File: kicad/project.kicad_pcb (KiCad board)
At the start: 2 copper layers, 59 x 59 mm, 36 parts, among them J1 Conn_01x05, J2 Conn_01x01, SW1 SW_SPDT, SW2 SW_SPDT, SW3 SW_Push, U1 STM32L031F4Px

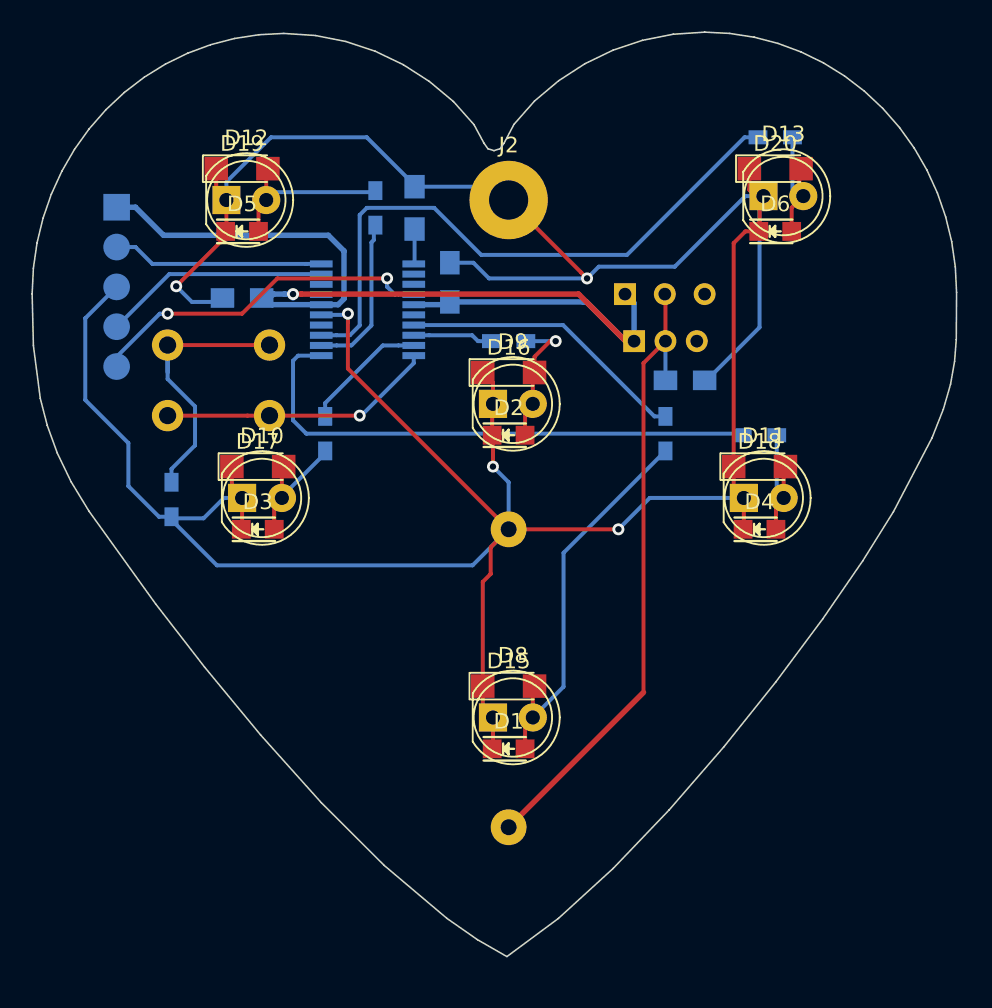
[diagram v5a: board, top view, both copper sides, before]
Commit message: Reverse polarity protection
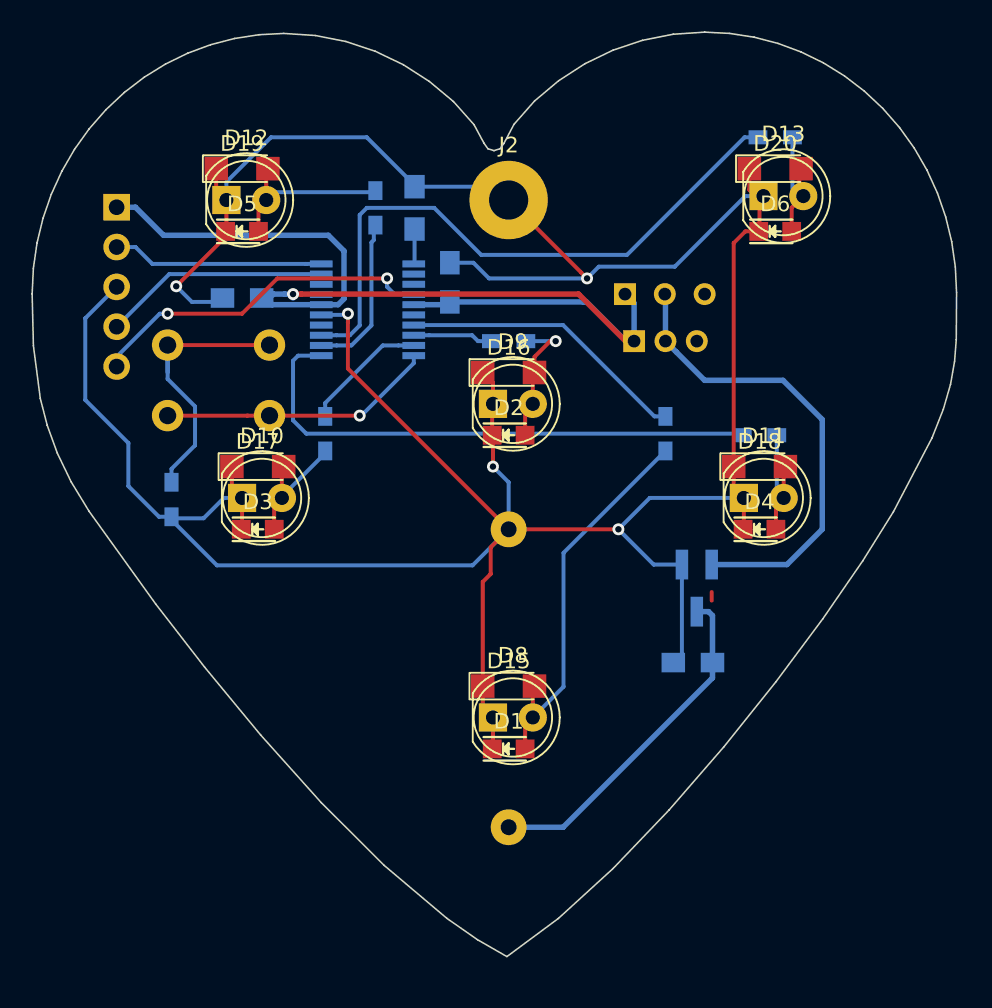
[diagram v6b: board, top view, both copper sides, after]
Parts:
- added Q1: SI2323CDS, TO_SOT_Packages_SMD:SOT-23_Handsoldering, B.Cu at (142.0, 120.8)
- J1: footprint SWD_Header -> Pin_Headers:Pin_Header_Straight_1x05_Pitch2.54mm
- moved C1 18.0 mm to (141.8, 125.5), turned to 180 degrees
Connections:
- SW1 pad 2: /BATT+ -> /BATT_PROTECTED
- SW2 pad 2: /BATT+ -> /BATT_PROTECTED
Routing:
- net /BATT_PROTECTED: track 0.00 -> 30.1 mm
- net /BATT+: track 40.7 -> 22.0 mm
- net GND: track 215.2 -> 213.6 mm
- net (no net): track 0.00 -> 0.55 mm

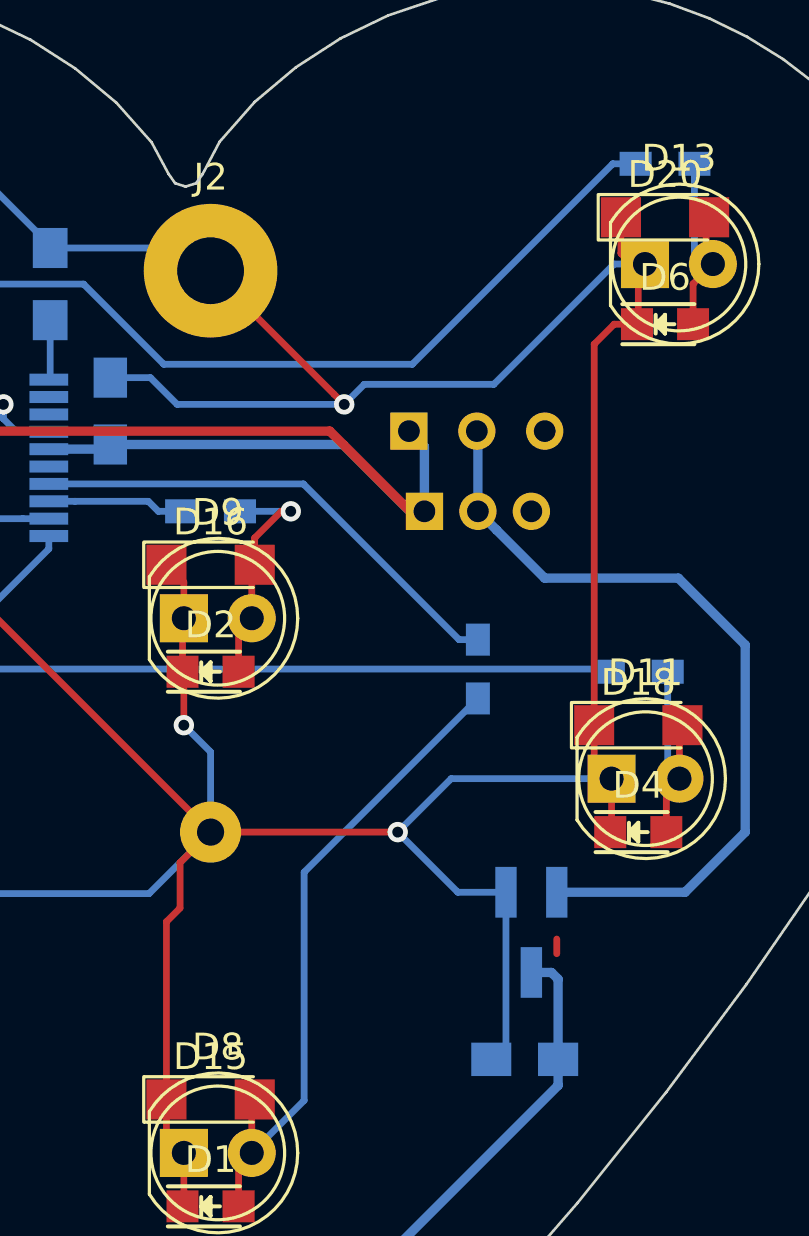
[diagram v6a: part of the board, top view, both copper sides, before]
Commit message: Cap after switch
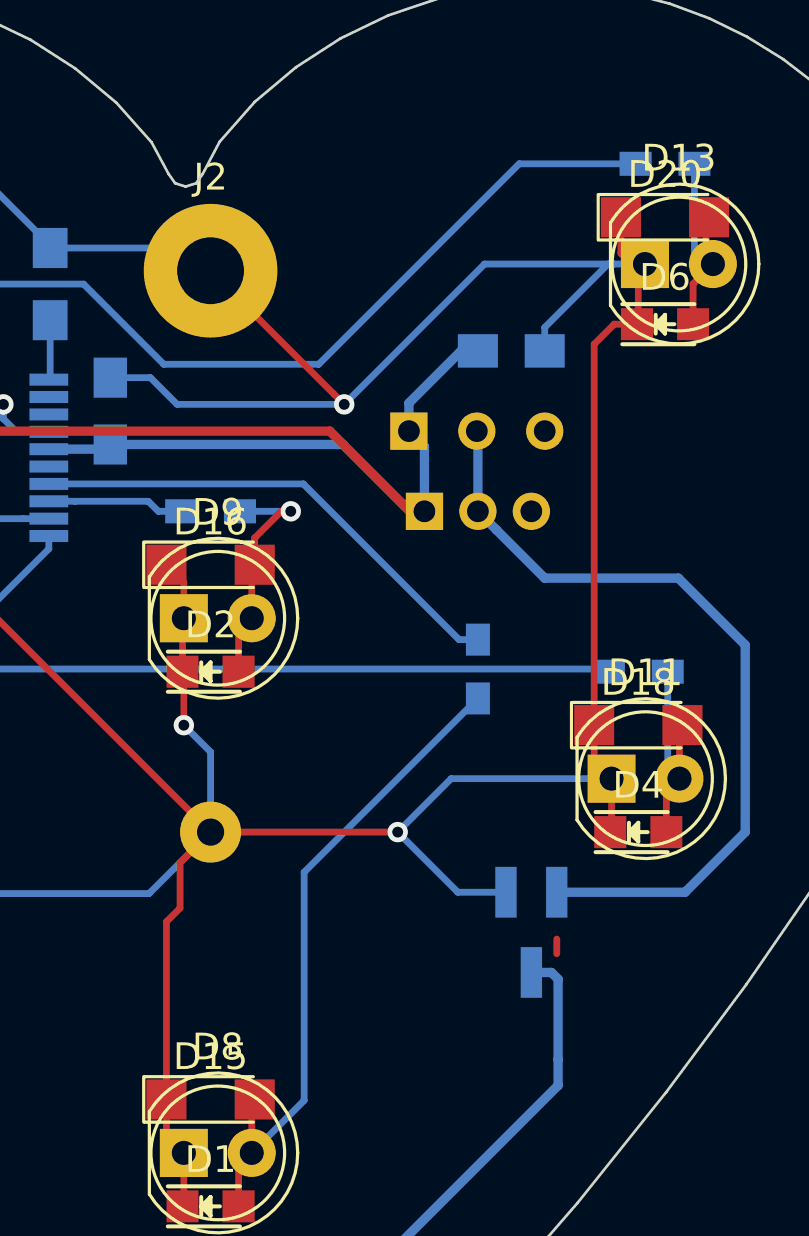
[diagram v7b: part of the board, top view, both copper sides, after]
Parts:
- moved C1 26.5 mm to (141.2, 99.0), turned to 0 degrees
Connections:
- C1 pad 1: /BATT+ -> BATT_SW
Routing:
- net BATT_SW: track 66.4 -> 70.9 mm
- net GND: track 213.6 -> 211.6 mm
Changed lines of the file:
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@@
-(kicad_pcb (version 4) (host pcbnew 4.0.7-e2-6376~58~ubuntu16.04.1)
+(kicad_pcb (version 4) (host pcbnew 4.0.6)
   (general
     (links 69)
-    (no_connects 0)
+    (no_connects 1)
     (area 99.561516 85.244019 158.615741 144.300151)
     (thickness 1.6)
     (drawings 89)
-    (tracks 238)
+    (tracks 242)
     (zones 0)
     (modules 37)
@@
   )
   (module Capacitors_SMD:C_0805_HandSoldering (layer B.Cu)
-    (at 141.75 125.5 180)
+    (at 141.25 99)
     (descr "Capacitor SMD 0805, hand soldering")
     (tags "capacitor 0805")
     (attr smd)
-    (fp_text reference C1 (at 0 2.1 180) (layer B.SilkS)
-      (effects (font (size 1 1) (thickness 0.15)) (justify mirror))
-    )
-    (fp_text value 10UF (at 0 -2.1 180) (layer B.Fab)
+    (fp_text reference C1 (at 0 2.1) (layer B.SilkS)
+      (effects (font (size 1 1) (thickness 0.15)) (justify mirror))
+    )
+    (fp_text value 10UF (at 0 -2.1) (layer B.Fab)
       (effects (font (size 1 1) (thickness 0.15)) (justify mirror))
     )
@@
     (fp_line (start 0.5 0.85) (end -0.5 0.85) (layer B.SilkS) (width 0.15))
     (fp_line (start -0.5 -0.85) (end 0.5 -0.85) (layer B.SilkS) (width 0.15))
-    (pad 1 smd rect (at -1.25 0 180) (size 1.5 1.25) (layers B.Cu B.Paste B.Mask)
-      (net 24 /BATT+))
-    (pad 2 smd rect (at 1.25 0 180) (size 1.5 1.25) (layers B.Cu B.Paste B.Mask)
+    (pad 1 smd rect (at -1.25 0) (size 1.5 1.25) (layers B.Cu B.Paste B.Mask)
+      (net 25 BATT_SW))
+    (pad 2 smd rect (at 1.25 0) (size 1.5 1.25) (layers B.Cu B.Paste B.Mask)
       (net 1 GND))
     (model Capacitors_SMD.3dshapes/C_0805_HandSoldering.wrl
@@
   (gr_line (start 142.50999 85.29402) (end 140.495258 85.427179) (layer Edge.Cuts) (width 0.1))
   (segment (start 142.95 121) (end 142.95 121.55) (width 0.254) (layer F.Cu) (net 0))
-  (segment (start 141.05 119.25) (end 141.05 124.95) (width 0.254) (layer B.Cu) (net 1))
-  (segment (start 141.05 124.95) (end 140.5 125.5) (width 0.254) (layer B.Cu) (net 1))
+  (segment (start 142.5 99) (end 142.5 98.121) (width 0.254) (layer B.Cu) (net 1))
+  (segment (start 142.5 98.121) (end 144.871 95.75) (width 0.254) (layer B.Cu) (net 1))
+  (segment (start 144.871 95.75) (end 145.096 95.75) (width 0.254) (layer B.Cu) (net 1))
+  (segment (start 145.096 95.75) (end 146.25 95.75) (width 0.254) (layer B.Cu) (net 1))
   (segment (start 141.05 119.25) (end 139.25 119.25) (width 0.254) (layer B.Cu) (net 1))
   (segment (start 139.25 119.25) (end 137 117) (width 0.254) (layer B.Cu) (net 1))
@@
   (segment (start 127.75 100) (end 128.75 101) (width 0.254) (layer B.Cu) (net 1))
   (segment (start 128.75 101) (end 135 101) (width 0.254) (layer B.Cu) (net 1))
-  (segment (start 146.25 95.75) (end 145.096 95.75) (width 0.254) (layer B.Cu) (net 1))
-  (segment (start 135.75 100.25) (end 135 101) (width 0.254) (layer B.Cu) (net 1))
-  (segment (start 145.096 95.75) (end 140.596 100.25) (width 0.254) (layer B.Cu) (net 1))
-  (segment (start 140.596 100.25) (end 135.75 100.25) (width 0.254) (layer B.Cu) (net 1))
+  (segment (start 140.25 95.75) (end 135 101) (width 0.254) (layer B.Cu) (net 1))
+  (segment (start 145.096 95.75) (end 145.096 95.75) (width 0.254) (layer B.Cu) (net 1))
+  (segment (start 145.096 95.75) (end 140.25 95.75) (width 0.254) (layer B.Cu) (net 1))
   (segment (start 146 96) (end 146 97.95098) (width 0.254) (layer F.Cu) (net 1))
   (segment (start 146 97.95098) (end 145.95098 98) (width 0.254) (layer F.Cu) (net 1))
@@
   (segment (start 119.975 105.275) (end 119.029 105.275) (width 0.254) (layer B.Cu) (net 11))
   (segment (start 119.029 105.275) (end 118.05 105.275) (width 0.254) (layer B.Cu) (net 11))
-  (segment (start 145.9 92) (end 145.046 92) (width 0.254) (layer B.Cu) (net 12))
-  (segment (start 145.046 92) (end 137.546 99.5) (width 0.254) (layer B.Cu) (net 12))
-  (segment (start 137.546 99.5) (end 128.25 99.5) (width 0.254) (layer B.Cu) (net 12))
+  (segment (start 145.9 92) (end 141.546 92) (width 0.254) (layer B.Cu) (net 12))
+  (segment (start 141.546 92) (end 134.046 99.5) (width 0.254) (layer B.Cu) (net 12))
+  (segment (start 134.046 99.5) (end 128.25 99.5) (width 0.254) (layer B.Cu) (net 12))
   (segment (start 128.25 99.5) (end 125.25 96.5) (width 0.254) (layer B.Cu) (net 12))
   (segment (start 125.25 96.5) (end 120.955638 96.5) (width 0.254) (layer B.Cu) (net 12))
@@
   (segment (start 148.04902 98) (end 148.04902 96.49098) (width 0.254) (layer F.Cu) (net 22))
   (segment (start 148.04902 96.49098) (end 148.54 96) (width 0.254) (layer F.Cu) (net 22))
+  (segment (start 142.75 122.25) (end 142 122.25) (width 0.35) (layer B.Cu) (net 24))
+  (segment (start 130 136) (end 133.475 136) (width 0.35) (layer B.Cu) (net 24))
+  (segment (start 133.475 136) (end 143 126.475) (width 0.35) (layer B.Cu) (net 24))
   (segment (start 143 125.5) (end 143 122.5) (width 0.35) (layer B.Cu) (net 24))
   (segment (start 143 122.5) (end 142.75 122.25) (width 0.35) (layer B.Cu) (net 24))
-  (segment (start 142.75 122.25) (end 142 122.25) (width 0.35) (layer B.Cu) (net 24))
-  (segment (start 130 136) (end 133.475 136) (width 0.35) (layer B.Cu) (net 24))
   (segment (start 143 126.475) (end 143 125.5) (width 0.35) (layer B.Cu) (net 24))
-  (segment (start 133.475 136) (end 143 126.475) (width 0.35) (layer B.Cu) (net 24))
+  (segment (start 137.42 102) (end 137.42 100.9515) (width 0.35) (layer B.Cu) (net 25))
+  (segment (start 137.42 100.9515) (end 139.3715 99) (width 0.35) (layer B.Cu) (net 25))
+  (segment (start 139.3715 99) (end 140 99) (width 0.35) (layer B.Cu) (net 25))
   (segment (start 115 102) (end 115.711185 102) (width 0.35) (layer B.Cu) (net 25))
   (segment (start 115.711185 102) (end 116.25 102) (width 0.35) (layer B.Cu) (net 25))

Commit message: Labels
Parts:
- J1: footprint Pin_Headers:Pin_Header_Straight_1x05_Pitch2.54mm -> SWD_Header
- moved D13 0.35 mm to (146.0, 96.0)
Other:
- board text added: "CLK"
- board text added: "DIO"
- board text added: "GND"
- board text added: "PWR"
- board text added: "RST"
